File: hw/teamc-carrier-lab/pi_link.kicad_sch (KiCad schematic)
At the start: 6 parts, among them J1 RPi GPIO ribbon, J13 UART console

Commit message: Carrier rev B (UPC lab): placed and routed on one copper layer, DRC 0/0/0
- place_carrier_lab.py: fixed floorplan (power right, J1 centre, SP4 socket top-left
  edge, UI leads left edge, fuel gauge bottom-left); provisional 100 x 80 mm outline
  until the box is measured.
- linkroute.py: single-layer grid router whose second "layer" is straight wire links
  (bare wire on the component side between two unplated holes).
- route_carrier_lab.py: hand-coded power path, SCK swap under R84/R83, left half; the
  rest routed in a topology order, --search over the band-net orders.
- finish_carrier_lab.py: GND pour (0.4 mm), FR10 no-fill areas, M3 keep-outs, ground
  island joins, links -> W parts (one-pin symbol, WireLink footprint with jumper pads).
- fab_carrier_lab.py: F.Cu + Edge.Cuts gerbers, drill, 1:1 copper PDFs, assembly and
  schematic PDFs, zip; renders; build_bom.py --rev b -> hw/BOM_revB.csv (~EUR 139).
- Schematic changes for one layer (documented on the sheets and in DESIGN_NOTES):
  1206 R/C, no UI pull-ups, 4 x SMF5.0A instead of SP0504, R80 to 3V3_RADIO, no R81,
  no C71/TP10/TP2 (C12 10 uF), 3V3_PI from J1 pin 1, FG_ALRT not routed, LED return
  on pin 25, J1 GND pins 20/30/34/39 unused, J23 on BAT_IN.
- ERC 0; DRC 0 violations / 0 unconnected / 0 parity (silk/mask checks off: the lab
  board has neither); 10 wire links (138 mm).

Co-Authored-By: Claude Opus 5.5 <noreply@anthropic.com>
Claude-Session: https://claude.ai/code/session_01M3xdFsssmBw3o2iBWKaKwo
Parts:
- added W1: wire link 34.5 mm, teamc:WireLink_L34.5mm, symbol Connector_Generic:Conn_01x01
- added W10, W6: wire link 5.0 mm, teamc:WireLink_L5.0mm, symbol Connector_Generic:Conn_01x01
- added W2: wire link 8.0 mm, teamc:WireLink_L8.0mm, symbol Connector_Generic:Conn_01x01
- added W3: wire link 8.5 mm, teamc:WireLink_L8.5mm, symbol Connector_Generic:Conn_01x01
- added W4: wire link 13.0 mm, teamc:WireLink_L13.0mm, symbol Connector_Generic:Conn_01x01
- added W5: wire link 19.5 mm, teamc:WireLink_L19.5mm, symbol Connector_Generic:Conn_01x01
- added W7: wire link 18.5 mm, teamc:WireLink_L18.5mm, symbol Connector_Generic:Conn_01x01
- added W8: wire link 15.0 mm, teamc:WireLink_L15.0mm, symbol Connector_Generic:Conn_01x01
- added W9: wire link 10.5 mm, teamc:WireLink_L10.5mm, symbol Connector_Generic:Conn_01x01
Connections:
- net 3V3_PI: now also J1.1 (Pin_1), W1.1 (Pin_1); no longer J1.17 (Pin_17)
- net GND: now also W2.1 (Pin_1), W3.1 (Pin_1); no longer J1.20 (Pin_20), J1.25 (Pin_25), J1.30 (Pin_30), J1.34 (Pin_34), J1.39 (Pin_39)
- net RADIO_CSN: now also W4.1 (Pin_1)
- net RADIO_IRQ: now also W5.1 (Pin_1), W6.1 (Pin_1)
- net SW_MODE_MRM: now also W7.1 (Pin_1)
- net SW_MODE_NM: now also W10.1 (Pin_1), W8.1 (Pin_1), W9.1 (Pin_1)
- net FG_ALRT: no longer names the net of J1.22 (Pin_22)
- new net LED_RTN: J1.25 (Pin_25)
- no-connect marks 12 -> 17
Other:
- note added: "1 3V3 (rev B: pin 1 feeds 3V3_PI)"
- note added: "17 3V3 (rev B: unused, pin 1 instead)"
- note added: "20 GND (rev B: not used on the carrier)"
- note added: "22 GPIO 25 (rev A FG_ALRT; not routed in rev B)"
- note added: "25 GND (rev B: the LEDs' return only)"
- note added: "30 GND (rev B: not used on the carrier)"
- note added: "34 GND (rev B: not used on the carrier)"
- note added: "39 GND (rev B: not used on the carrier)"
- note added: "WIRE LINKS (rev B, single copper layer): bare 0.6 mm tinned copper wire on the component side between two unplated 1.0 mm holes, soldered on the copper side; the board's crossings. Positions and lengths: hw/teamc-carrier-lab/links.json."
- note removed: "1 3V3 (unused: pin 17 feeds the pull-ups)"
- note removed: "17 3V3"
- note removed: "20 GND"
- note removed: "22 GPIO 25"
- note removed: "25 GND"
- note removed: "30 GND"
- note removed: "34 GND"
- note removed: "39 GND"

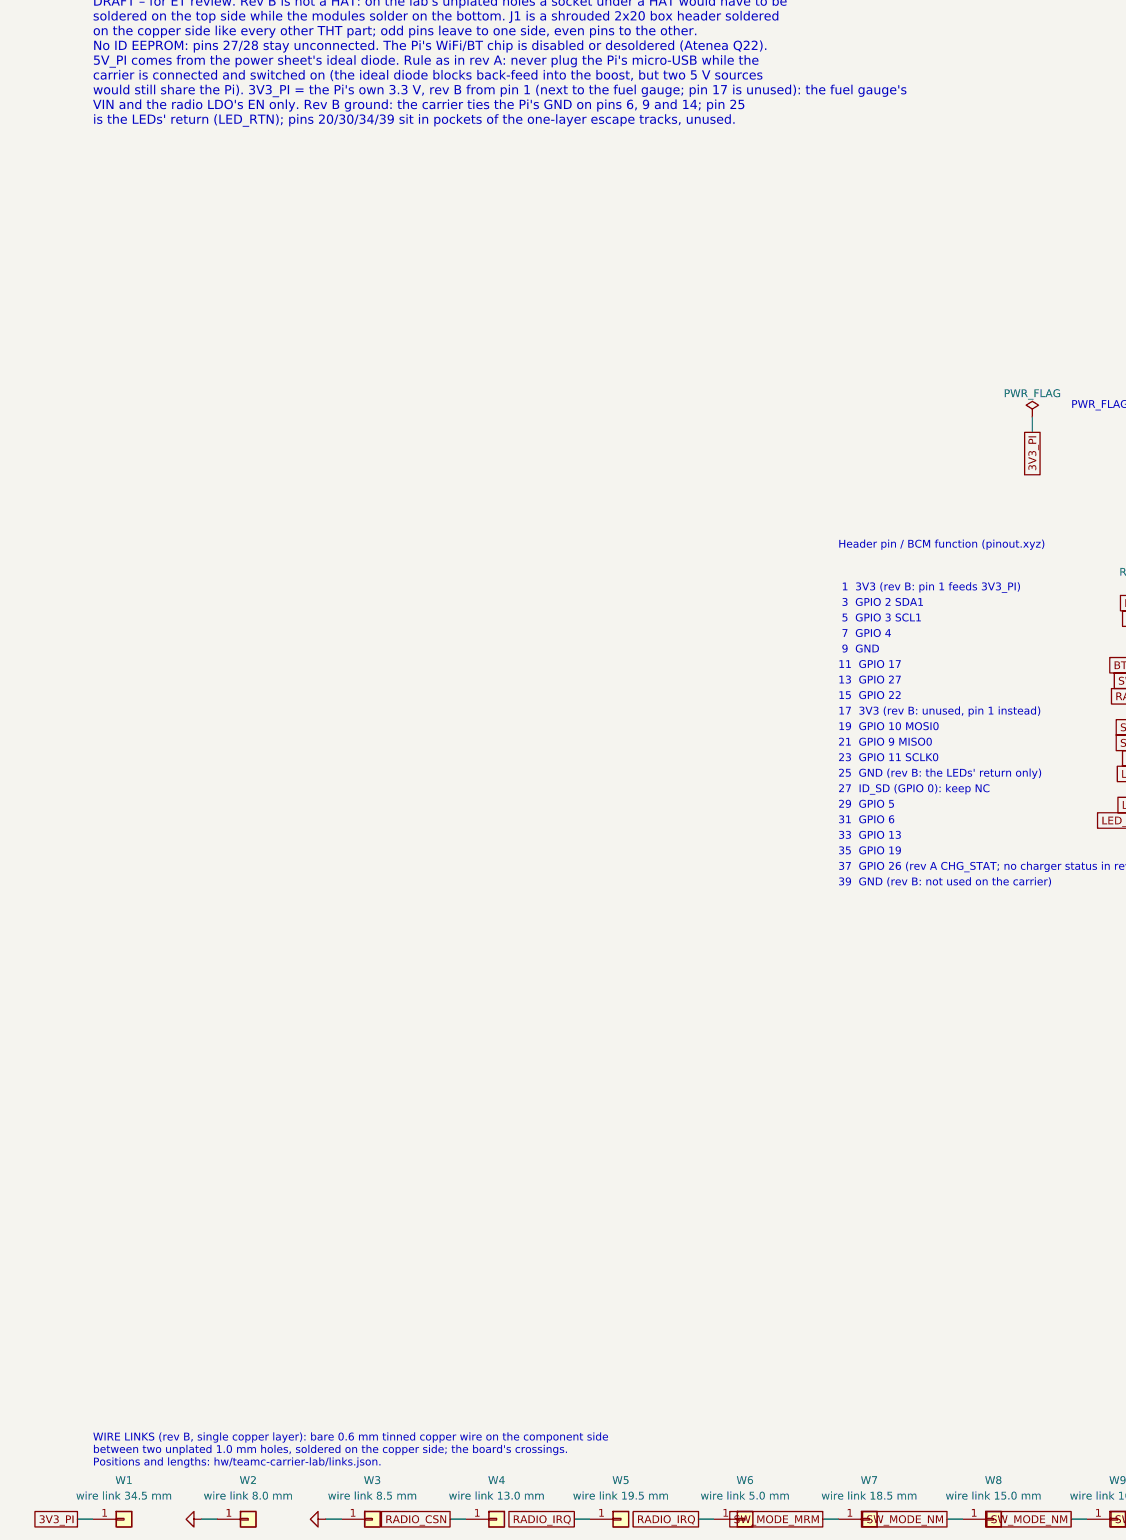
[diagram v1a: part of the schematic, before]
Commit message: Carrier rev B review fixes: charger on VBAT, insulated links, SPI at 4 MHz
- J23 (TP4056 lead) back on VBAT behind F1/Q1: placed between the VBAT line and
  C5, GND to C5's ground pad, R1 now returns to J20's GND pin. A reversed cell no
  longer reaches the charger and the lead is fused.
- Wire links: insulated 22 AWG solid hook-up wire, not bare (schematic note, W
  MPN, WireLink footprint text, BoM, shopping list).
- Ribbon grounds: tying J1 20/25 to the pour was tried; the inner pocket of J1's
  escape ring (LEDs, pins 20/25) has no legal wire link, the outer pockets would
  cost 3 more. Kept as before and SPI defaults to 4 MHz instead (teamc-node
  --spi-hz, NRF24_LINUX_CFG_DEFAULT; was 8 MHz) until T2 is clean; flying-wire
  fallback documented.
- Pipeline rerun twice: ERC 0, DRC 0/0/0, one copper layer, no vias, 10 links;
  fab zip, 1:1 PDFs, renders and BOM_revB.csv (EUR 139.01) regenerated.
- fw 318, proto all scenarios + 116 usb, linux builds, phy_config OK.

Co-Authored-By: Claude Opus 5.5 <noreply@anthropic.com>
Claude-Session: https://claude.ai/code/session_01PKzvcoWGaf5niy6TrXYsya
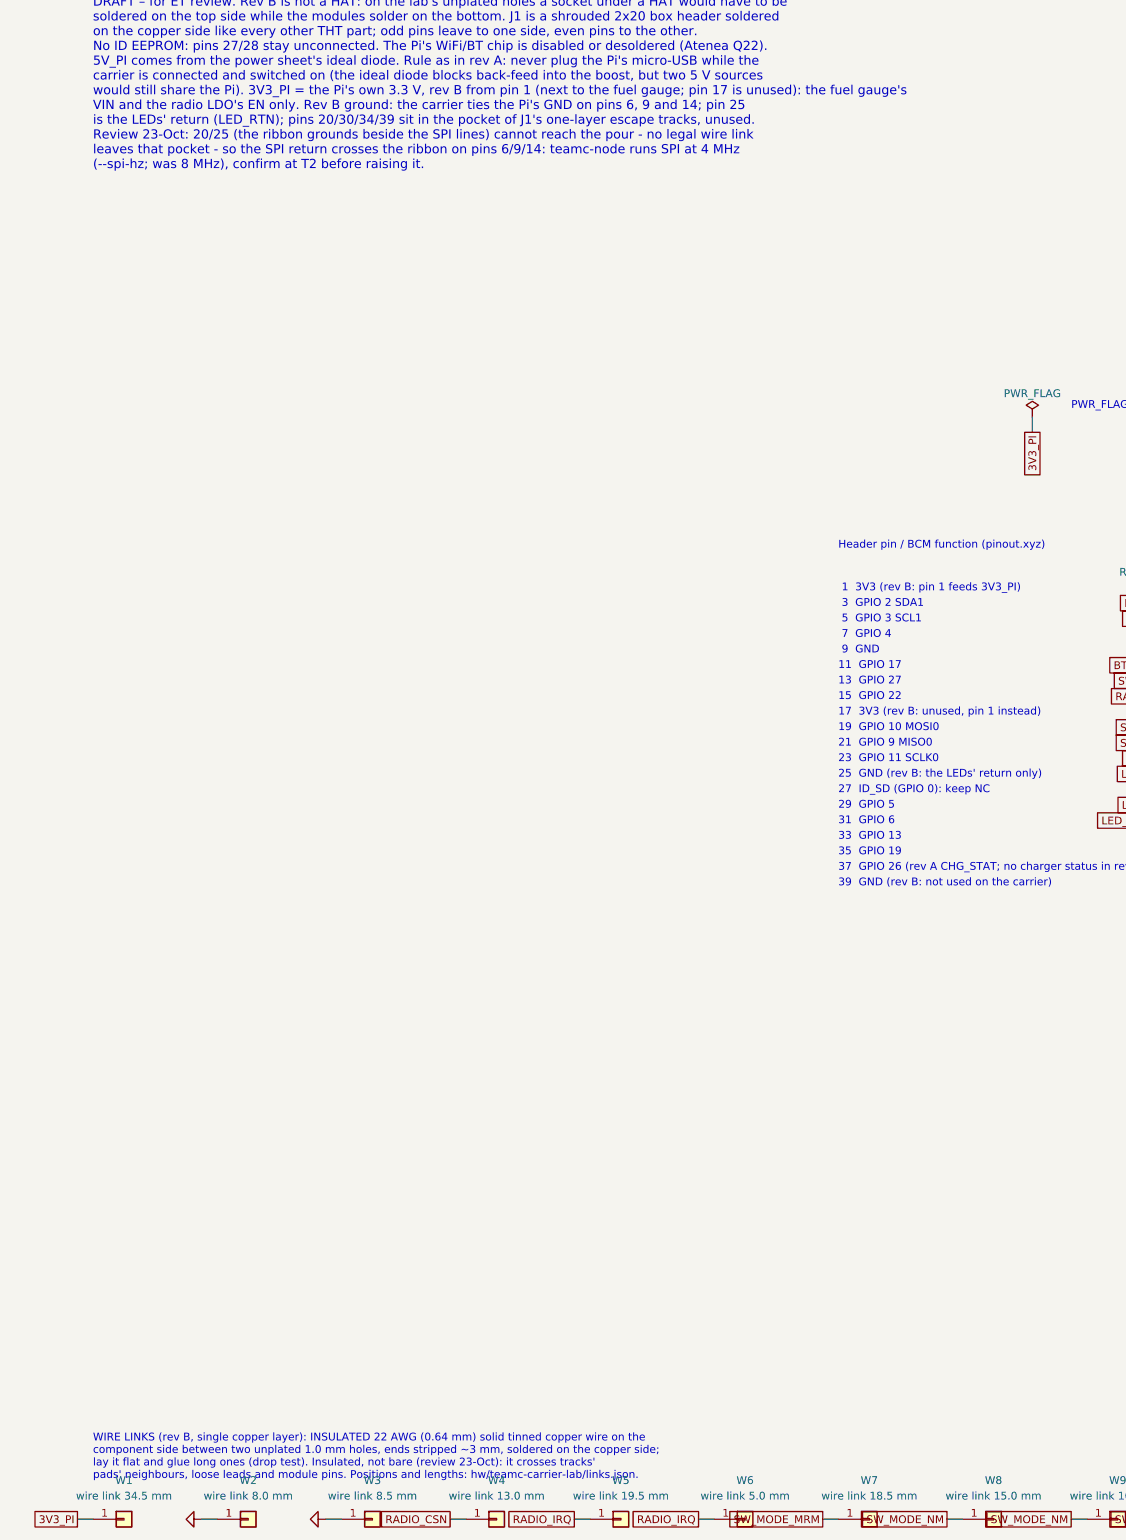
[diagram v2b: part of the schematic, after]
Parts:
- W1, W10, W2, W3, W4, W5, W6, W7, W8, W9: MPN 0.6 mm (22 AWG) tinned copper wire, bare -> 22 AWG solid tinned copper hook-up wire, PVC/PTFE insulated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
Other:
- note added: "WIRE LINKS (rev B, single copper layer): INSULATED 22 AWG (0.64 mm) solid tinned copper wire on the component side between two unplated 1.0 mm holes, ends stripped ~3 mm, soldered on the copper side; lay it flat and glue long ones (drop test). Insulated, not bare (review 23-Oct): it crosses tracks' pads' neighbours, loose leads and module pins. Positions and lengths: hw/teamc-carrier-lab/links.js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"
- note removed: "WIRE LINKS (rev B, single copper layer): bare 0.6 mm tinned copper wire on the component side between two unplated 1.0 mm holes, soldered on the copper side; the board's crossings. Positions and lengths: hw/teamc-carrier-lab/links.json."
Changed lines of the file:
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@@
 			)
 		)
-		(property "MPN" "0.6 mm (22 AWG) tinned copper wire, bare"
+		(property "MPN" "22 AWG solid tinned copper hook-up wire, PVC/PTFE insulated (ends stripped)"
 			(at 30.48 276.86 0)
 			(effects
@@
 			)
 		)
-		(property "MPN" "0.6 mm (22 AWG) tinned copper wire, bare"
+		(property "MPN" "22 AWG solid tinned copper hook-up wire, PVC/PTFE insulated (ends stripped)"
 			(at 50.8 276.86 0)
 			(effects
@@
 			)
 		)
-		(property "MPN" "0.6 mm (22 AWG) tinned copper wire, bare"
+		(property "MPN" "22 AWG solid tinned copper hook-up wire, PVC/PTFE insulated (ends stripped)"
 			(at 71.12 276.86 0)
 			(effects
@@
 			)
 		)
-		(property "MPN" "0.6 mm (22 AWG) tinned copper wire, bare"
+		(property "MPN" "22 AWG solid tinned copper hook-up wire, PVC/PTFE insulated (ends stripped)"
 			(at 91.44 276.86 0)
 			(effects
@@
 			)
 		)
-		(property "MPN" "0.6 mm (22 AWG) tinned copper wire, bare"
+		(property "MPN" "22 AWG solid tinned copper hook-up wire, PVC/PTFE insulated (ends stripped)"
 			(at 111.76 276.86 0)
 			(effects
@@
 			)
 		)
-		(property "MPN" "0.6 mm (22 AWG) tinned copper wire, bare"
+		(property "MPN" "22 AWG solid tinned copper hook-up wire, PVC/PTFE insulated (ends stripped)"
 			(at 132.08 276.86 0)
 			(effects
@@
 			)
 		)
-		(property "MPN" "0.6 mm (22 AWG) tinned copper wire, bare"
+		(property "MPN" "22 AWG solid tinned copper hook-up wire, PVC/PTFE insulated (ends stripped)"
 			(at 152.4 276.86 0)
 			(effects
@@
 			)
 		)
-		(property "MPN" "0.6 mm (22 AWG) tinned copper wire, bare"
+		(property "MPN" "22 AWG solid tinned copper hook-up wire, PVC/PTFE insulated (ends stripped)"
 			(at 172.72 276.86 0)
 			(effects
@@
 			)
 		)
-		(property "MPN" "0.6 mm (22 AWG) tinned copper wire, bare"
+		(property "MPN" "22 AWG solid tinned copper hook-up wire, PVC/PTFE insulated (ends stripped)"
 			(at 193.04 276.86 0)
 			(effects
@@
 			)
 		)
-		(property "MPN" "0.6 mm (22 AWG) tinned copper wire, bare"
+		(property "MPN" "22 AWG solid tinned copper hook-up wire, PVC/PTFE insulated (ends stripped)"
 			(at 213.36 276.86 0)
 			(effects
@@
 		)
 	)
-	(text "DRAFT – for ET review. Rev B is not a HAT: on the lab's unplated holes a socket under a HAT would have to be\nsoldered on the top side while the modules solder on the bottom. J1 is a shrouded 2x20 box header soldered\non the copper side like every other THT part; odd pins leave to one side, even pins to the other.\nNo ID EEPROM: pins 27/28 stay unconnected. The Pi's WiFi/BT chip is disabled or desoldered (Atenea Q22).\n5V_PI comes from the power sheet's ideal diode. Rule as in rev A: never plug the Pi's micro-USB while the\ncarrier is connected and switched on (the ideal diode blocks back-feed into the boost, but two 5 V sources\nwould still share the Pi). 3V3_PI = the Pi's own 3.3 V, rev B from pin 1 (next to the fuel gauge; pin 17 is unused): the fuel gauge's\nVIN and the radio LDO's EN only. Rev B ground: the carrier ties the Pi's GND on pins 6, 9 and 14; pin 25\nis the LEDs' return (LED_RTN); pins 20/30/34/39 sit in pockets of the one-layer escape tracks, unused."
+	(text "DRAFT – for ET review. Rev B is not a HAT: on the lab's unplated holes a socket under a HAT would have to be\nsoldered on the top side while the modules solder on the bottom. J1 is a shrouded 2x20 box header soldered\non the copper side like every other THT part; odd pins leave to one side, even pins to the other.\nNo ID EEPROM: pins 27/28 stay unconnected. The Pi's WiFi/BT chip is disabled or desoldered (Atenea Q22).\n5V_PI comes from the power sheet's ideal diode. Rule as in rev A: never plug the Pi's micro-USB while the\ncarrier is connected and switched on (the ideal diode blocks back-feed into the boost, but two 5 V sources\nwould still share the Pi). 3V3_PI = the Pi's own 3.3 V, rev B from pin 1 (next to the fuel gauge; pin 17 is unused): the fuel gauge's\nVIN and the radio LDO's EN only. Rev B ground: the carrier ties the Pi's GND on pins 6, 9 and 14; pin 25\nis the LEDs' return (LED_RTN); pins 20/30/34/39 sit in the pocket of J1's one-layer escape tracks, unused.\nReview 23-Oct: 20/25 (the ribbon grounds beside the SPI lines) cannot reach the pour - no legal wire link\nleaves that pocket - so the SPI return crosses the ribbon on pins 6/9/14: teamc-node runs SPI at 4 MHz\n(--spi-hz; was 8 MHz), confirm at T2 before raising it."
 		(exclude_from_sim no)
 		(at 25.4 27.94 0)
@@
 		)
 	)
-	(text "WIRE LINKS (rev B, single copper layer): bare 0.6 mm tinned copper wire on the component side\nbetween two unplated 1.0 mm holes, soldered on the copper side; the board's crossings.\nPositions and lengths: hw/teamc-carrier-lab/links.json."
+	(text "WIRE LINKS (rev B, single copper layer): INSULATED 22 AWG (0.64 mm) solid tinned copper wire on the\ncomponent side between two unplated 1.0 mm holes, ends stripped ~3 mm, soldered on the copper side;\nlay it flat and glue long ones (drop test). Insulated, not bare (review 23-Oct): it crosses tracks'\npads' neighbours, loose leads and module pins. Positions and lengths: hw/teamc-carrier-lab/links.json."
 		(exclude_from_sim no)
 		(at 25.4 262.89 0)
